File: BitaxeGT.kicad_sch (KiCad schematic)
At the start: 10 parts

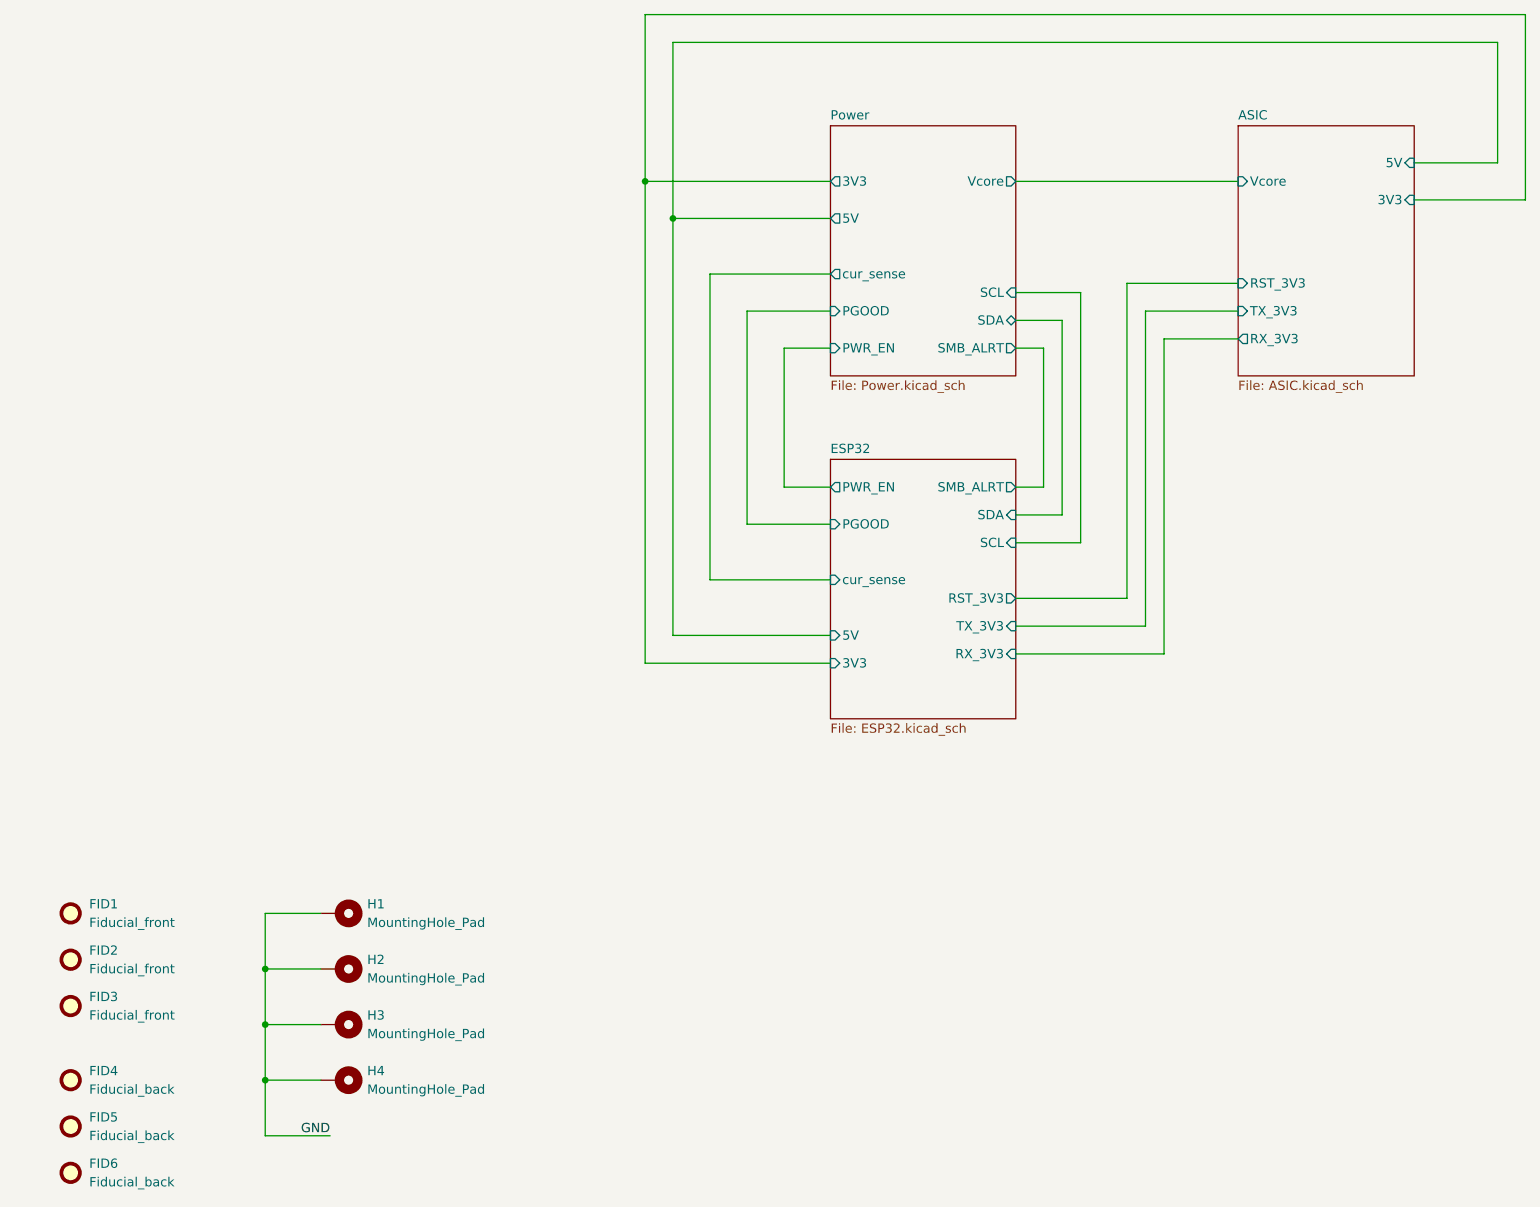
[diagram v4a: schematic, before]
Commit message: add fan chip
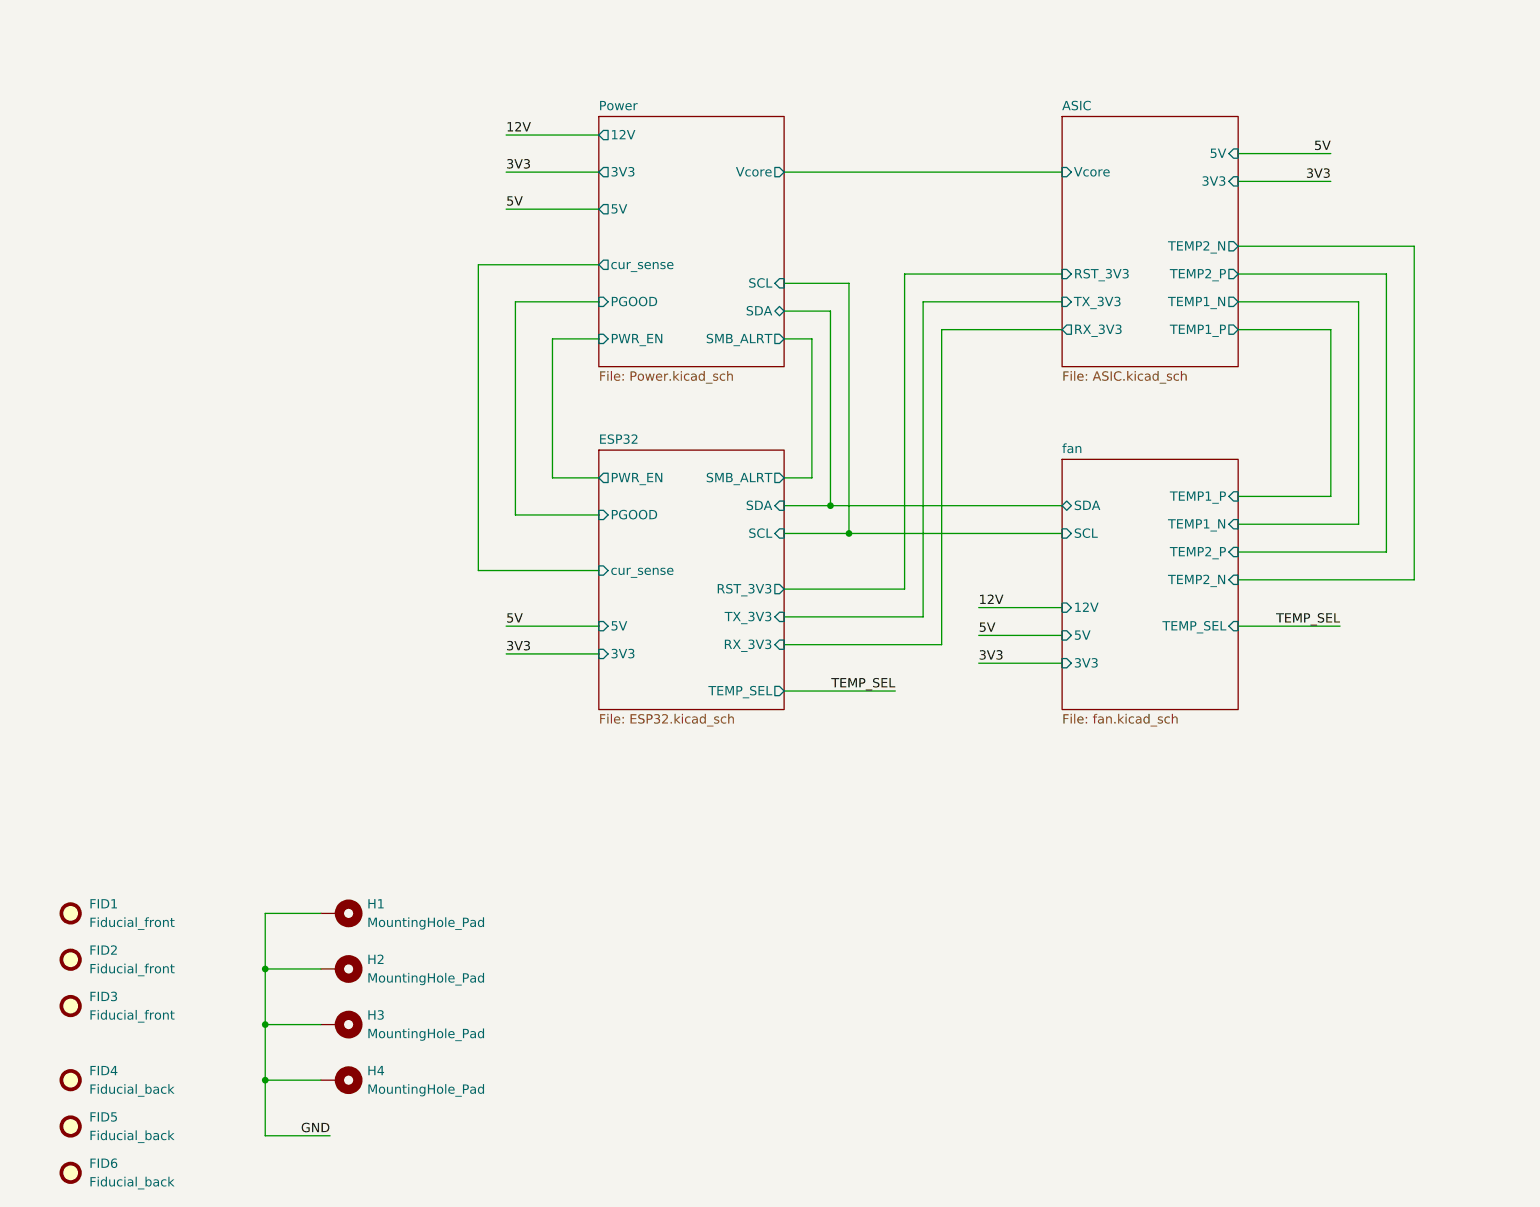
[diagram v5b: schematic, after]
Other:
- added sheet fan (fan.kicad_sch)
- sheet ASIC ports: added TEMP1_N, TEMP1_P, TEMP2_N, TEMP2_P; removed none
- sheet ESP32 ports: added TEMP_SEL; removed none
- sheet Power ports: added 12V; removed none

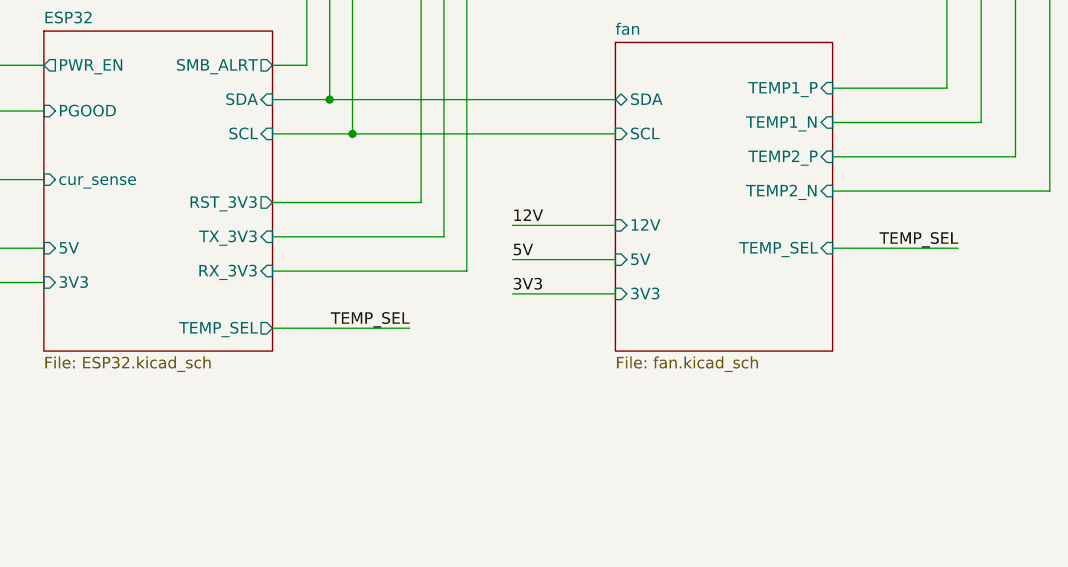
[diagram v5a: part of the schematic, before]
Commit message: change fan controller to EMC2103-2 with two temperature inputs
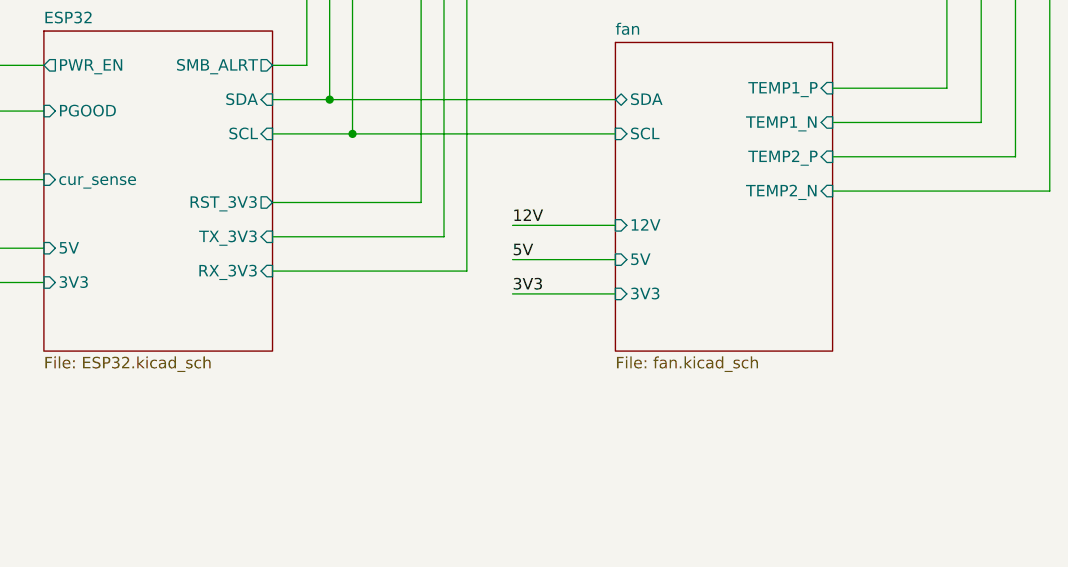
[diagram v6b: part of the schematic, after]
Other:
- sheet ESP32 ports: added none; removed TEMP_SEL
- sheet fan ports: added none; removed TEMP_SEL
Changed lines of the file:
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@@
-	(wire
-		(pts
-			(xy 204.47 113.03) (xy 218.44 113.03)
-		)
-		(stroke
-			(width 0)
-			(type default)
-		)
-	)
 	(wire
 		(pts
@@
 		(pts
 			(xy 71.12 167.64) (xy 71.12 175.26)
-		)
-		(stroke
-			(width 0)
-			(type default)
-		)
-	)
-	(wire
-		(pts
-			(xy 142.24 121.92) (xy 157.48 121.92)
 		)
 		(stroke
@@
 		)
 	)
-	(label "TEMP_SEL"
-		(at 218.44 113.03 180)
-		(fields_autoplaced yes)
-		(effects
-			(font
-				(size 1.27 1.27)
-			)
-			(justify right bottom)
-		)
-	)
 	(label "3V3"
 		(at 217.17 52.07 180)
-		(fields_autoplaced yes)
-		(effects
-			(font
-				(size 1.27 1.27)
-			)
-			(justify right bottom)
-		)
-	)
-	(label "TEMP_SEL"
-		(at 157.48 121.92 180)
 		(fields_autoplaced yes)
 		(effects
@@
 			)
 		)
-		(pin "TEMP_SEL" output
-			(at 142.24 121.92 0)
-			(effects
-				(font
-					(size 1.27 1.27)
-				)
-				(justify right)
-			)
-		)
 		(instances
 			(project "BitaxeGT"
@@
 			)
 		)
-		(pin "TEMP_SEL" input
-			(at 204.47 113.03 0)
-			(effects
-				(font
-					(size 1.27 1.27)
-				)
-				(justify right)
-			)
-		)

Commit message: create PCB, add components and heatsink
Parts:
- added HS1: Heatsink, bitaxe:Heatsink-BitaxeGT, symbol Mechanical:Heatsink
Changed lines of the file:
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@@
+	)
+	(symbol
+		(lib_id "Mechanical:Heatsink")
+		(at 120.65 171.45 0)
+		(unit 1)
+		(exclude_from_sim yes)
+		(in_bom yes)
+		(on_board yes)
+		(dnp no)
+		(fields_autoplaced yes)
+		(property "Reference" "HS1"
+			(at 124.46 168.2749 0)
+			(effects
+				(font
+					(size 1.27 1.27)
+				)
+				(justify left)
+			)
+		)
+		(property "Value" "Heatsink"
+			(at 124.46 170.8149 0)
+			(effects
+				(font
+					(size 1.27 1.27)
+				)
+				(justify left)
+			)
+		)
+		(property "Footprint" "bitaxe:Heatsink-BitaxeGT"
+			(at 120.9548 171.45 0)
+			(effects
+				(font
+					(size 1.27 1.27)
+				)
+				(hide yes)
+			)
+		)
+		(property "Datasheet" "~"
+			(at 120.9548 171.45 0)
+			(effects
+				(font
+					(size 1.27 1.27)
+				)
+				(hide yes)
+			)
+		)
+		(property "Description" "Heatsink"
+			(at 120.65 171.45 0)
+			(effects
+				(font
+					(size 1.27 1.27)
+				)
+				(hide yes)
+			)
+		)
+		(instances
+			(project ""
+				(path "/61fe8d2c-9301-4ad9-8caf-c47acfa835b0"
+					(reference "HS1")
+					(unit 1)
+				)
+			)
+		)
 	)
 	(symbol

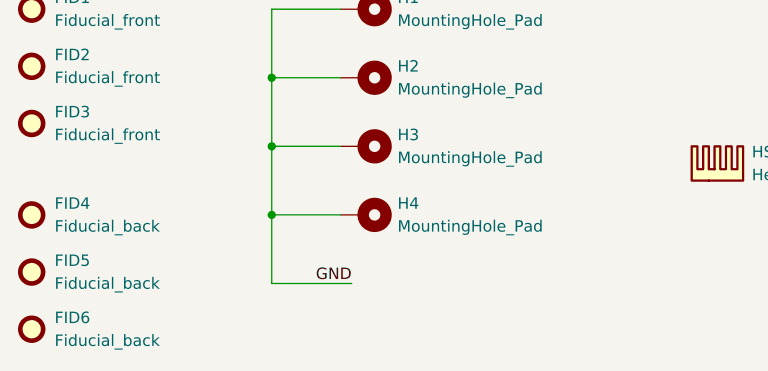
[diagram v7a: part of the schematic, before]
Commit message: Route main power paths
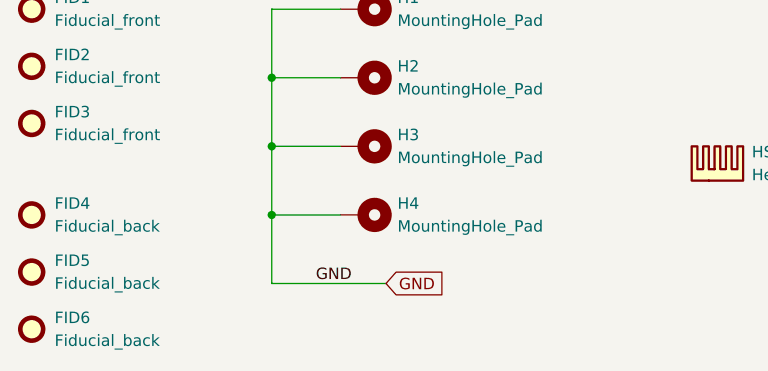
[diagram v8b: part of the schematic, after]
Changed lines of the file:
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@@
 	(wire
 		(pts
-			(xy 71.12 182.88) (xy 80.01 182.88)
+			(xy 71.12 182.88) (xy 83.82 182.88)
 		)
 		(stroke
@@
 		)
 	)
+	(global_label "GND"
+		(shape input)
+		(at 83.82 182.88 0)
+		(fields_autoplaced yes)
+		(effects
+			(font
+				(size 1.27 1.27)
+			)
+			(justify left)
+		)
+		(property "Intersheetrefs" "${INTERSHEET_REFS}"
+			(at 90.6757 182.88 0)
+			(effects
+				(font
+					(size 1.27 1.27)
+				)
+				(justify left)
+				(hide yes)
+			)
+		)
+	)
